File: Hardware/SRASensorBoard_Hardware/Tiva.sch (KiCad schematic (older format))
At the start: 8 parts

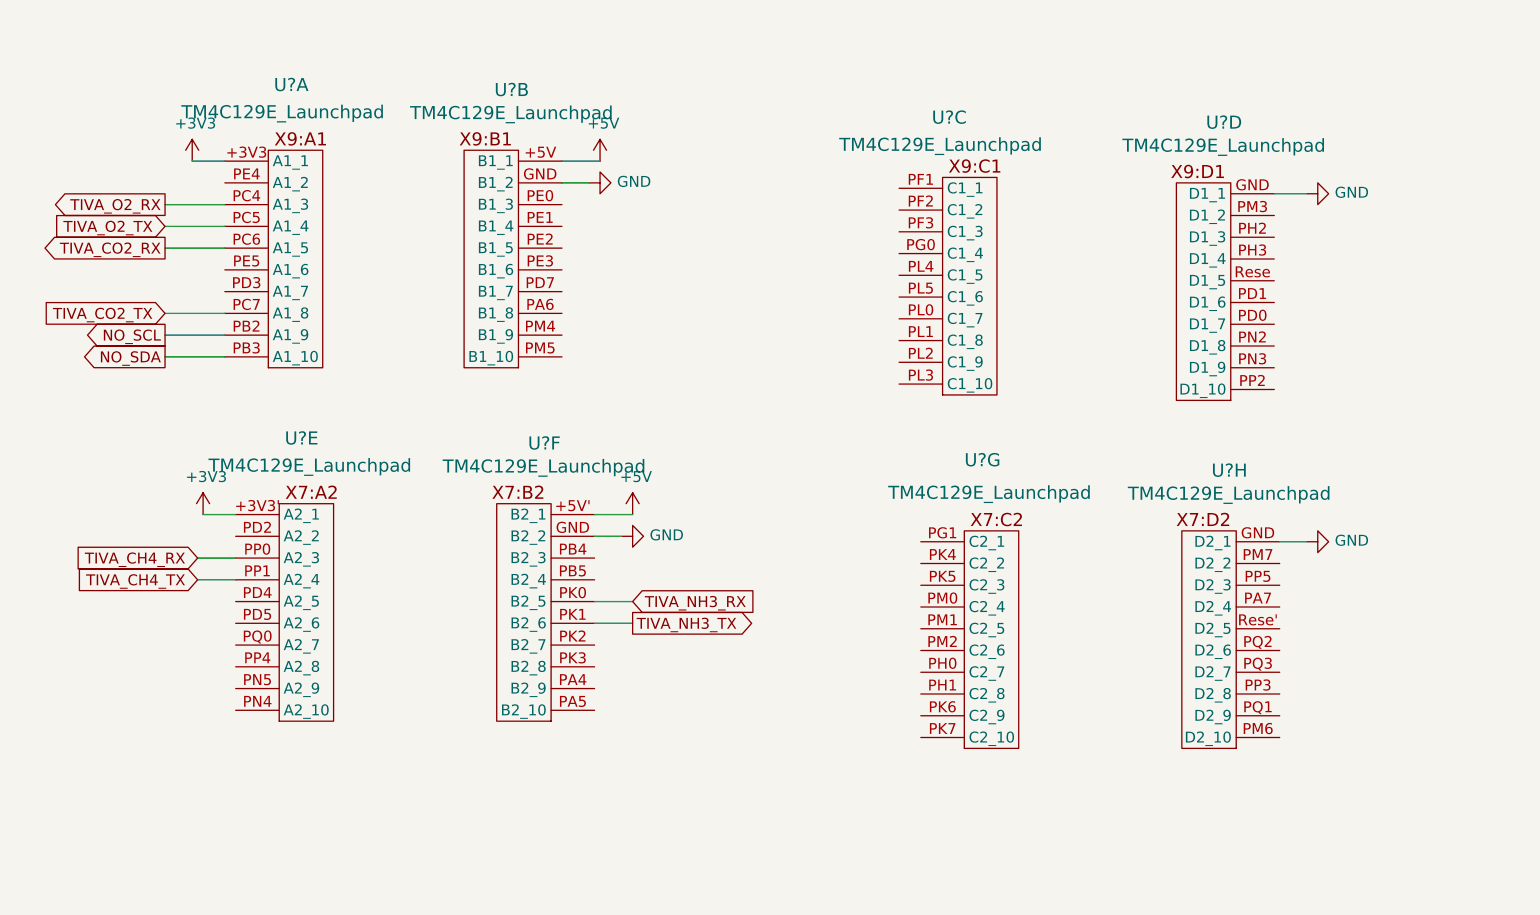
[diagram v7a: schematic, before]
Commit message: Added software pins and no connects to Tiva
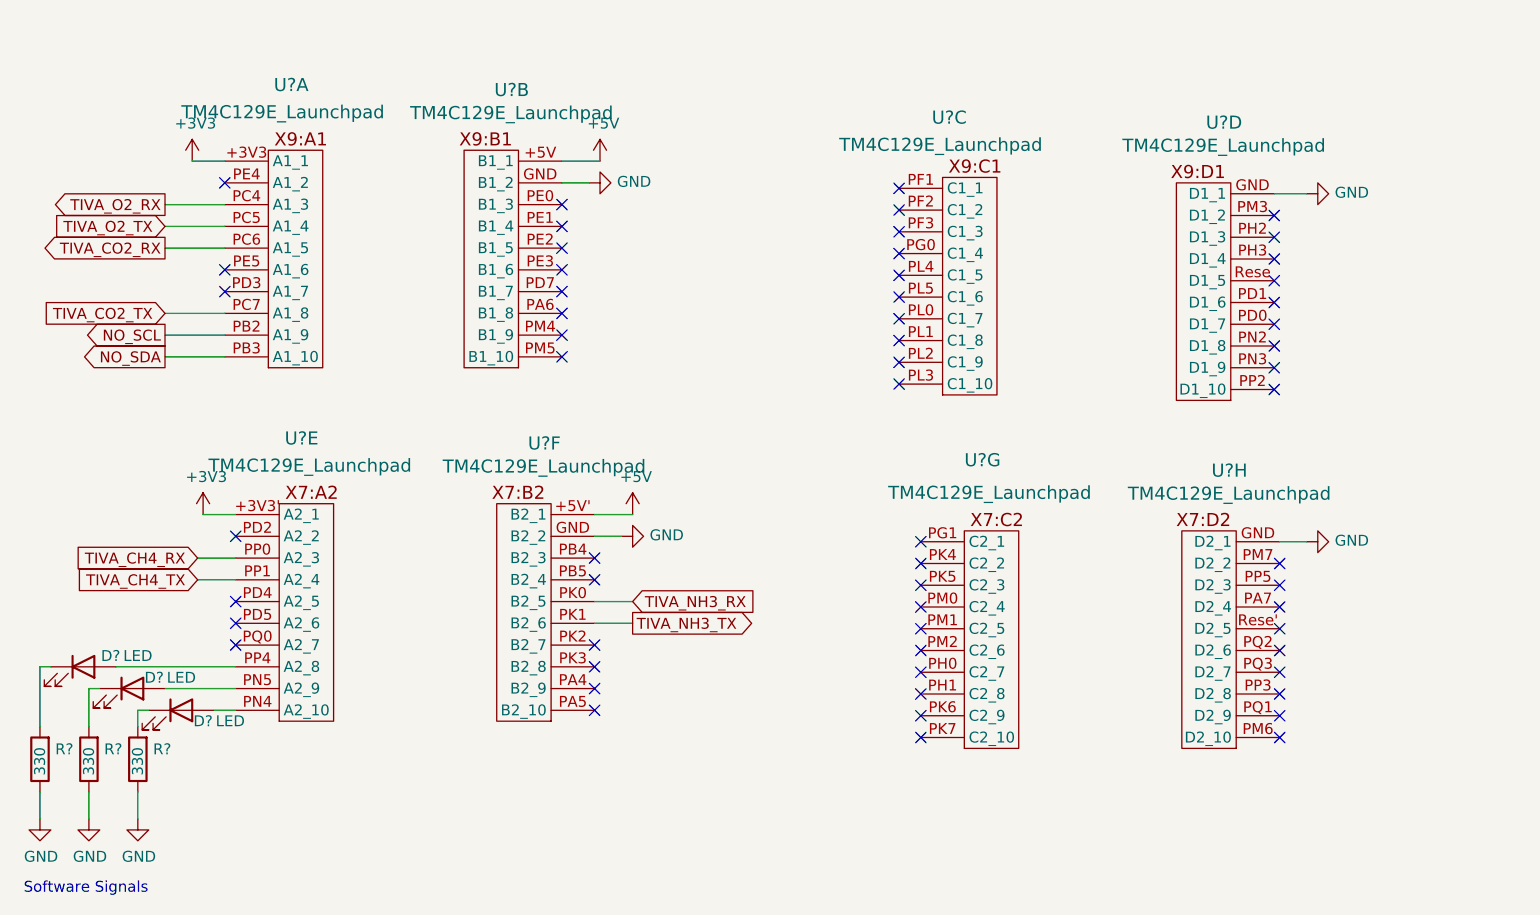
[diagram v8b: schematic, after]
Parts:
- added D? (x3): LED, symbol Device:LED
- added R? (x3): 330, symbol Device:R
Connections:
- net GND: now also R?.1, R?.1, R?.1
- net at U?.PN4 (A2_10): now also D?.2 (A)
- net at U?.PN5 (A2_9): now also D?.2 (A)
- net at U?.PP4 (A2_8): now also D?.2 (A)
- new net: D?.1 (K), R?.2 (x3)
- no-connect marks 0 -> 59
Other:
- note added: "Software Signals"
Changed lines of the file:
@@
 Wire Wire Line
 	3825 3600 4000 3600
+NoConn ~ 2125 1575
+NoConn ~ 2125 1975
+NoConn ~ 2125 2075
+NoConn ~ 2175 3200
+NoConn ~ 2175 3500
+NoConn ~ 2175 3600
+NoConn ~ 2175 3700
+NoConn ~ 3825 4000
+NoConn ~ 3825 3900
+NoConn ~ 3825 3800
+NoConn ~ 3825 3700
+NoConn ~ 3825 3400
+NoConn ~ 3825 3300
+NoConn ~ 3675 2375
+NoConn ~ 3675 2275
+NoConn ~ 3675 2175
+NoConn ~ 3675 2075
+NoConn ~ 3675 1975
+NoConn ~ 3675 1875
+NoConn ~ 3675 1775
+NoConn ~ 3675 1675
+NoConn ~ 5225 1600
+NoConn ~ 5225 1700
+NoConn ~ 5225 1800
+NoConn ~ 5225 1900
+NoConn ~ 5225 2000
+NoConn ~ 5225 2100
+NoConn ~ 5225 2200
+NoConn ~ 5225 2300
+NoConn ~ 5225 2400
+NoConn ~ 5225 2500
+NoConn ~ 6950 2525
+NoConn ~ 6950 2425
+NoConn ~ 6950 2325
+NoConn ~ 6950 2225
+NoConn ~ 6950 2125
+NoConn ~ 6950 2025
+NoConn ~ 6950 1925
+NoConn ~ 6950 1825
+NoConn ~ 6950 1725
+NoConn ~ 5325 3225
+NoConn ~ 5325 3325
+NoConn ~ 5325 3425
+NoConn ~ 5325 3525
+NoConn ~ 5325 3625
+NoConn ~ 5325 3725
+NoConn ~ 5325 3825
+NoConn ~ 5325 3925
+NoConn ~ 5325 4025
+NoConn ~ 5325 4125
+NoConn ~ 6975 3325
+NoConn ~ 6975 3425
+NoConn ~ 6975 3525
+NoConn ~ 6975 3625
+NoConn ~ 6975 3725
+NoConn ~ 6975 3825
+NoConn ~ 6975 3925
+NoConn ~ 6975 4025
+NoConn ~ 6975 4125
+$Comp
+L Device:LED D?
+U 1 1 6165658F
+P 1700 3900
+F 0 "D?" H 1800 3950 50  0000 C CNN
+F 1 "LED" H 1925 3950 50  0000 C CNN
+F 2 "" H 1700 3900 50  0001 C CNN
+F 3 "~" H 1700 3900 50  0001 C CNN
+	1    1700 3900
+	1    0    0    -1
+$EndComp
+$Comp
+L Device:LED D?
+U 1 1 6165680B
+P 1925 4000
+F 0 "D?" H 2025 3950 50  0000 C CNN
+F 1 "LED" H 2150 3950 50  0000 C CNN
+F 2 "" H 1925 4000 50  0001 C CNN
+F 3 "~" H 1925 4000 50  0001 C CNN
+	1    1925 4000
+	1    0    0    -1
+$EndComp
+Wire Wire Line
+	2175 3800 1625 3800
+Wire Wire Line
+	1850 3900 2175 3900
+Wire Wire Line
+	2075 4000 2175 4000
+Wire Wire Line
+	1775 4000 1725 4000
+$Comp
+L Device:R R?
+U 1 1 6165A889
+P 1725 4225
+F 0 "R?" H 1655 4179 50  0000 R CNN
+F 1 "330" V 1725 4300 50  0000 R CNN
+F 2 "" V 1655 4225 50  0001 C CNN
+F 3 "~" H 1725 4225 50  0001 C CNN
+	1    1725 4225
+	-1   0    0    1
+$EndComp
+Wire Wire Line
+	1725 4000 1725 4075
+$Comp
+L Device:R R?
+U 1 1 6165C9F3
+P 1500 4225
+F 0 "R?" H 1430 4179 50  0000 R CNN
+F 1 "330" V 1500 4300 50  0000 R CNN
+F 2 "" V 1430 4225 50  0001 C CNN
+F 3 "~" H 1500 4225 50  0001 C CNN
+	1    1500 4225
+	-1   0    0    1
+$EndComp
+$Comp
+L Device:R R?
+U 1 1 6165CD26
+P 1275 4225
+F 0 "R?" H 1205 4179 50  0000 R CNN
+F 1 "330" V 1275 4300 50  0000 R CNN
+F 2 "" V 1205 4225 50  0001 C CNN
+F 3 "~" H 1275 4225 50  0001 C CNN
+	1    1275 4225
+	-1   0    0    1
+$EndComp
+$Comp
+L Device:LED D?
+U 1 1 616555A2
+P 1475 3800
+F 0 "D?" H 1600 3850 50  0000 C CNN
+F 1 "LED" H 1725 3850 50  0000 C CNN
+F 2 "" H 1475 3800 50  0001 C CNN
+F 3 "~" H 1475 3800 50  0001 C CNN
+	1    1475 3800
+	1    0    0    -1
+$EndComp
+Wire Wire Line
+	1550 3900 1500 3900
+Wire Wire Line
+	1500 3900 1500 4075
+Wire Wire Line
+	1325 3800 1275 3800
+Wire Wire Line
+	1275 3800 1275 4075
+$Comp
+L power:GND #PWR?
+U 1 1 61666E76
+P 1500 4500
+F 0 "#PWR?" H 1500 4250 50  0001 C CNN
+F 1 "GND" H 1505 4327 50  0000 C CNN
+F 2 "" H 1500 4500 50  0001 C CNN
+F 3 "" H 1500 4500 50  0001 C CNN
+	1    1500 4500
+	1    0    0    -1
+$EndComp
+$Comp
+L power:GND #PWR?
+U 1 1 6166AD67
+P 1725 4500
+F 0 "#PWR?" H 1725 4250 50  0001 C CNN
+F 1 "GND" H 1730 4327 50  0000 C CNN
+F 2 "" H 1725 4500 50  0001 C CNN
+F 3 "" H 1725 4500 50  0001 C CNN
+	1    1725 4500
+	1    0    0    -1
+$EndComp
+$Comp
+L power:GND #PWR?
+U 1 1 6166AEA5
+P 1275 4500
+F 0 "#PWR?" H 1275 4250 50  0001 C CNN
+F 1 "GND" H 1280 4327 50  0000 C CNN
+F 2 "" H 1275 4500 50  0001 C CNN
+F 3 "" H 1275 4500 50  0001 C CNN
+	1    1275 4500
+	1    0    0    -1
+$EndComp
+Wire Wire Line
+	1275 4375 1275 4500
+Wire Wire Line
+	1500 4375 1500 4500
+Wire Wire Line
+	1725 4375 1725 4500
+Text Notes 1200 4850 0    50   ~ 0
+Software Signals
 $EndSCHEMATC
